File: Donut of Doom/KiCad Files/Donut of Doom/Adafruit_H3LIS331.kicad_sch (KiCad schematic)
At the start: 7 parts, among them U3 H3LIS331DLTR

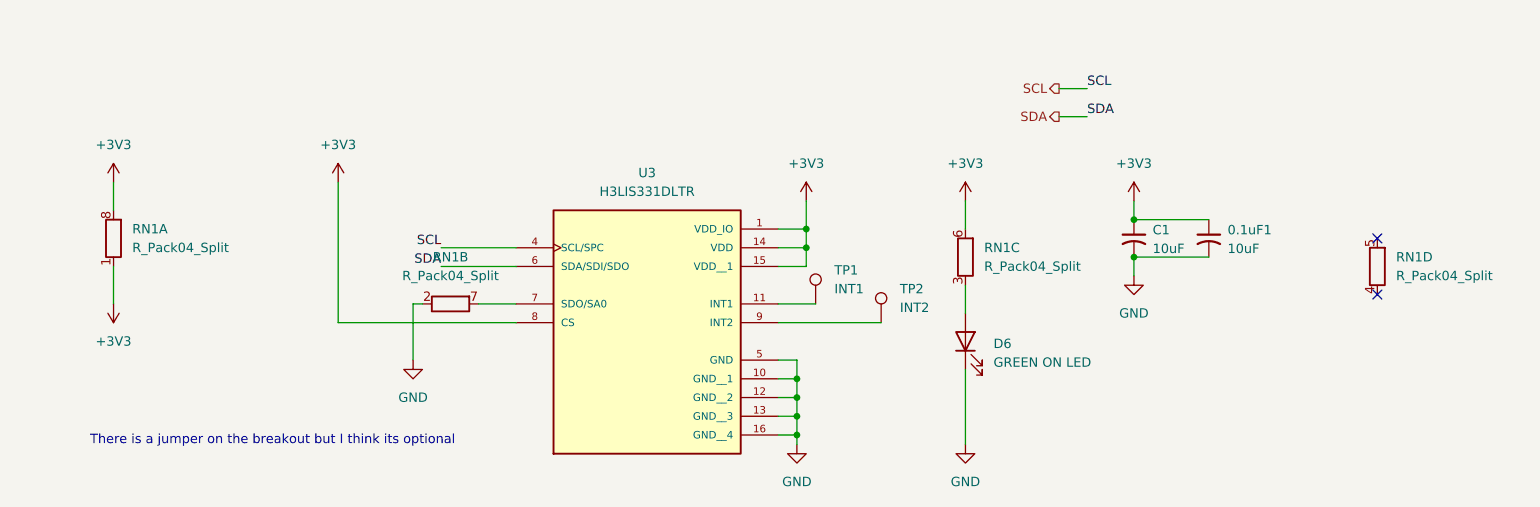
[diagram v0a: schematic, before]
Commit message: PCB almost finalized, awaiting dfm
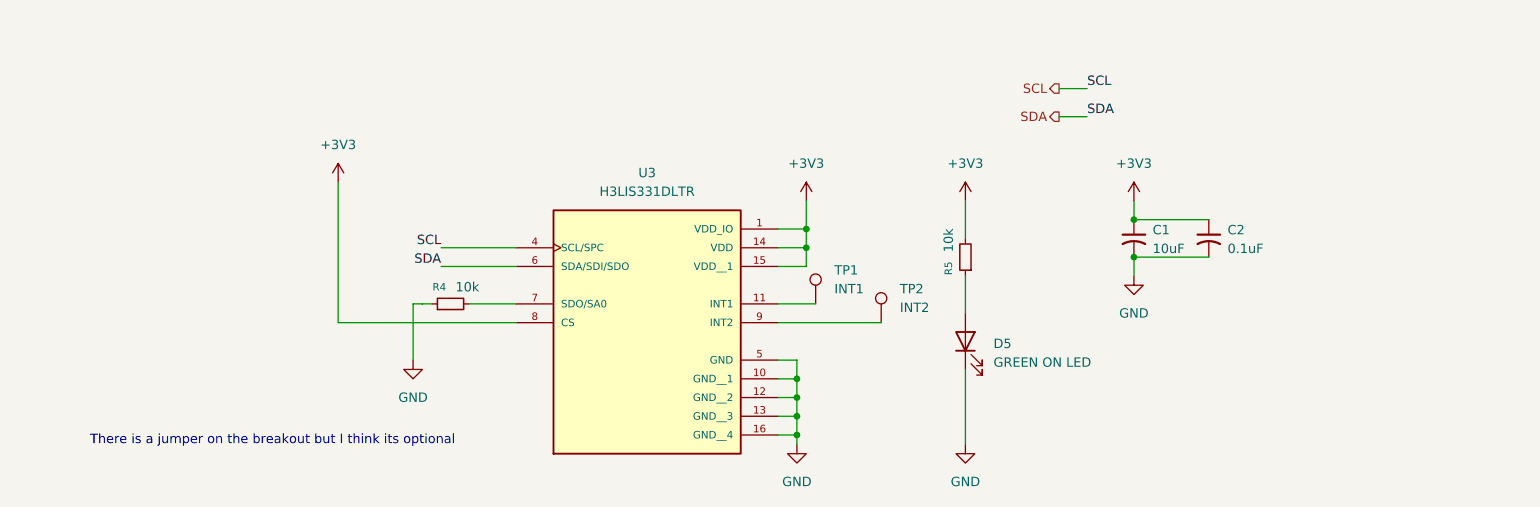
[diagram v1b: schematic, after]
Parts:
- removed RN1: R_Pack04_Split, Resistor_SMD:R_Array_Concave_4x0603, symbol Device:R_Pack04_Split
- added R4, R5: 10k, Resistor_SMD:R_0603_1608Metric_Pad0.98x0.95mm_HandSolder, symbol Device:R_Small
- C2: renamed from 0.1uF1; value 10uF -> 0.1uF
- renumbered D6 to D5
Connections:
- net +3V3: now also R5.2
- net GND: now also R4.1
- net at D5.2 (A): now also R5.1
- net at U3.7 (SDO/SA0): now also R4.2
- no-connect marks 2 -> 0

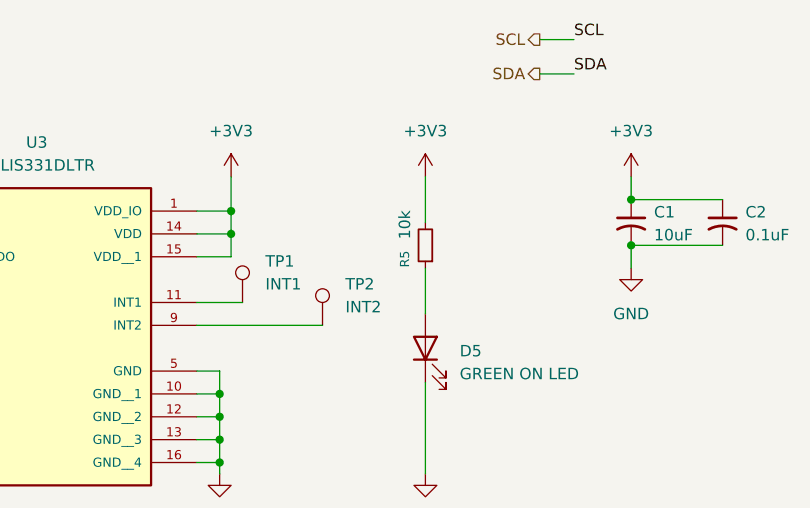
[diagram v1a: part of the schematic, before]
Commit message: fixed resistor values
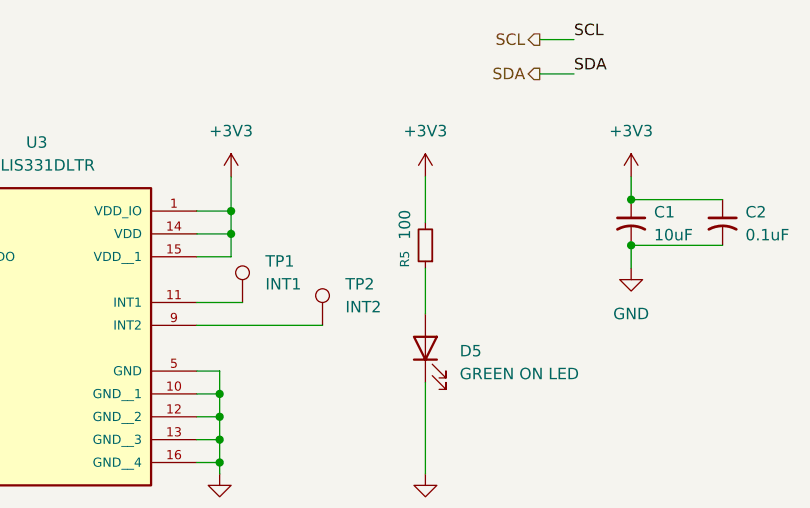
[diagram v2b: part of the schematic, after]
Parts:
- R5: value 10k -> 100
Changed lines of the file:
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@@
 			)
 		)
-		(property "Value" "10k"
+		(property "Value" "100"
 			(at 142.494 95.504 90)
 			(effects

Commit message: Added more breakouts, corrected MOSFET, better esc and led pads.
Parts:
- TP1, TP2: footprint TestPoint:TestPoint_Pad_1.5x1.5mm -> TestPoint:TestPoint_Pad_D1.5mm
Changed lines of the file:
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@@
+	(wire
+		(pts
+			(xy 64.77 99.06) (xy 83.82 99.06)
+		)
+		(stroke
+			(width 0)
+			(type default)
+		)
+	)
 	(wire
 		(pts
@@
 	(wire
 		(pts
+			(xy 64.77 96.52) (xy 83.82 96.52)
+		)
+		(stroke
+			(width 0)
+			(type default)
+		)
+	)
+	(wire
+		(pts
 			(xy 167.64 90.17) (xy 167.64 92.71)
 		)
@@
 	(wire
 		(pts
-			(xy 73.66 96.52) (xy 83.82 96.52)
-		)
-		(stroke
-			(width 0)
-			(type default)
-		)
-	)
-	(wire
-		(pts
 			(xy 167.64 97.79) (xy 177.8 97.79)
 		)
@@
 		(pts
 			(xy 167.64 97.79) (xy 167.64 100.33)
-		)
-		(stroke
-			(width 0)
-			(type default)
-		)
-	)
-	(wire
-		(pts
-			(xy 73.66 99.06) (xy 83.82 99.06)
 		)
 		(stroke
@@
 	)
 	(label "SDA"
-		(at 73.66 99.06 180)
+		(at 64.77 99.06 180)
 		(effects
 			(font
@@
 	)
 	(label "SCL"
-		(at 73.66 96.52 180)
+		(at 64.77 96.52 180)
 		(effects
 			(font
@@
 			)
 		)
-		(property "Footprint" "TestPoint:TestPoint_Pad_1.5x1.5mm"
+		(property "Footprint" "TestPoint:TestPoint_Pad_D1.5mm"
 			(at 138.43 106.68 0)
 			(effects
@@
 			)
 		)
-		(property "Footprint" "TestPoint:TestPoint_Pad_1.5x1.5mm"
+		(property "Footprint" "TestPoint:TestPoint_Pad_D1.5mm"
 			(at 129.54 104.14 0)
 			(effects

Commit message: Added 2nd accel, fixed mosfet, added more GND pads
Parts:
- removed TP1: INT1, TestPoint:TestPoint_Pad_D1.5mm, symbol Connector:TestPoint
- removed TP2: INT2, TestPoint:TestPoint_Pad_D1.5mm, symbol Connector:TestPoint
- renumbered D5 to D6, R4 to R6, R5 to R7
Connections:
- net INT2: now reaches U3.9 (INT2)
- net INT1: now reaches U3.11 (INT1)
